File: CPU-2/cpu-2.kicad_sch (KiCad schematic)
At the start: 141 parts, among them Q1 2N2369A, X1 14-Pin Socket, X2 14-Pin Socket, X3 14-Pin Socket, X4 14-Pin Socket, X5 14-Pin Socket, X6 14-Pin Socket

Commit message: Tidied up and added additional Project ORB documents + more KiCAD updates
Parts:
- added D8: 1N4001, Diode_THT:D_DO-41_SOD81_P10.16mm_Horizontal, symbol Sphere:1N4001
- added TSC1, TSC2, TSC3, TSC4, TSC5: ~, symbol Sphere:Jumper_Open
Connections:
- net +5V: now also E14.13 (1C), E25.13, E3.20 (V_{CC}), E3.25 (ENABLE), X1.14 (Φ_{2}), X4.7
- net GNDREF: now also E3.1 (VSS), X4.8, TSC5.
- net at E3.2 (PA0): now also X4.2
- net at E3.3 (PA1): now also X4.3
- net at E3.39 (CA2): now also X4.12
- net at E3.4 (PA2): now also X4.11
- net  32: now reaches E3.40 (CA1)
- net  32: now also TSC1., TSC2., TSC3., TSC4., TSC5.
- net at E3.5 (PA3): now also X4.4
- net at E3.6 (PA4): now also X4.10
- net at E3.7 (PA5): now also X4.5
- net at E3.8 (PA6): now also X4.6
- net at E3.9 (PA7): now also X4.9
- net at E7., E7.8 (Q_{C}): now also TSC3.
- net at E7.1 (CKB): now also E7.12 (Q_{A}), TSC1.
- net at E7.10 (GND): now also TSC4.
- net at E7.9 (Q_{B}): now also TSC2.
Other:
- note added: "RTC"
- moved on the sheet: C7, E3, E7

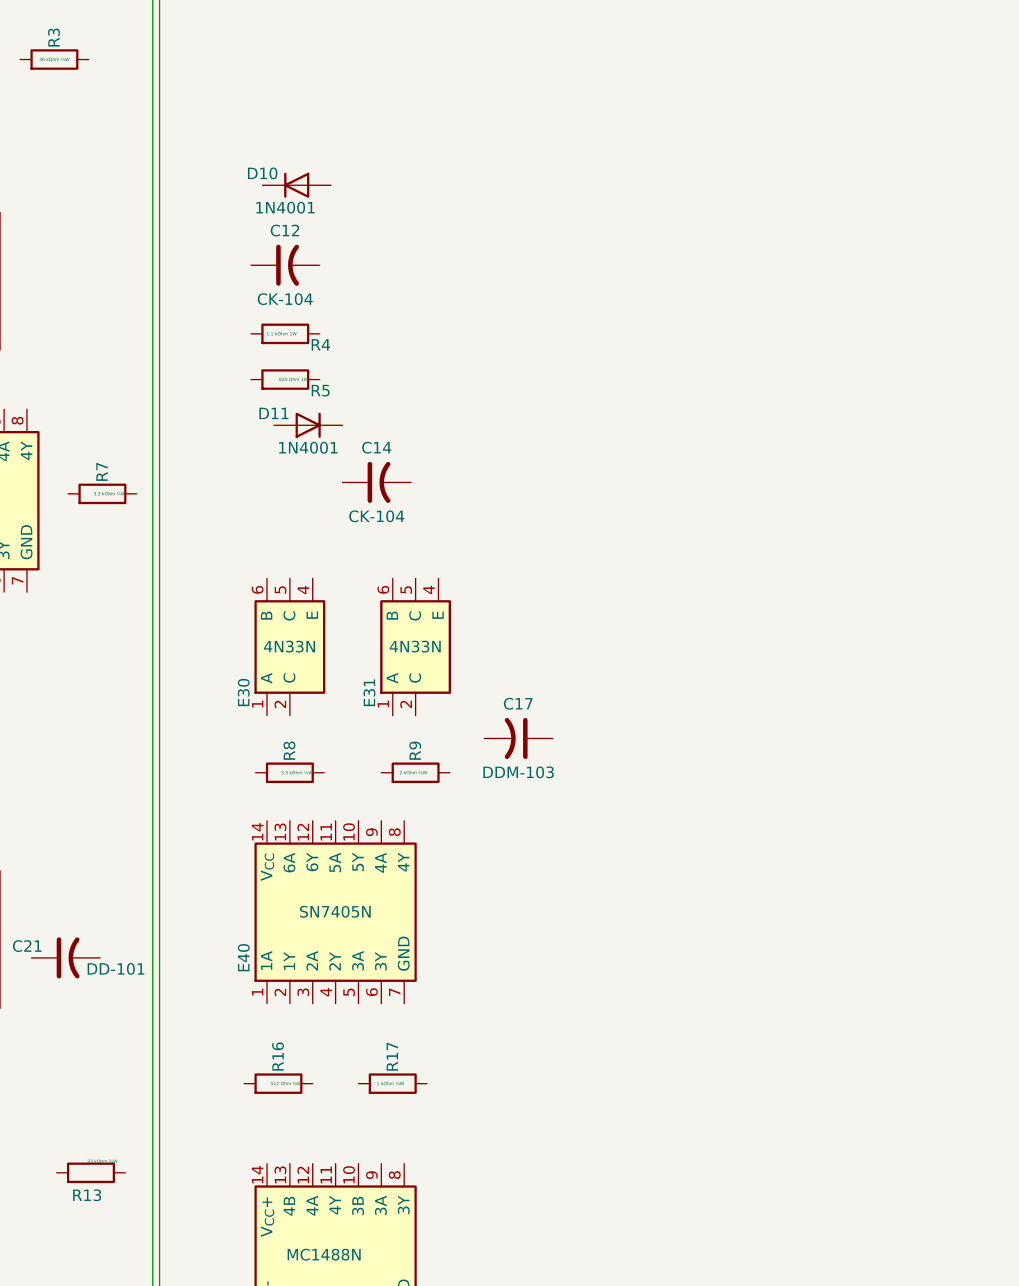
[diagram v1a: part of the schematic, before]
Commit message: Added Project ORB documents and latest KiCAD updates
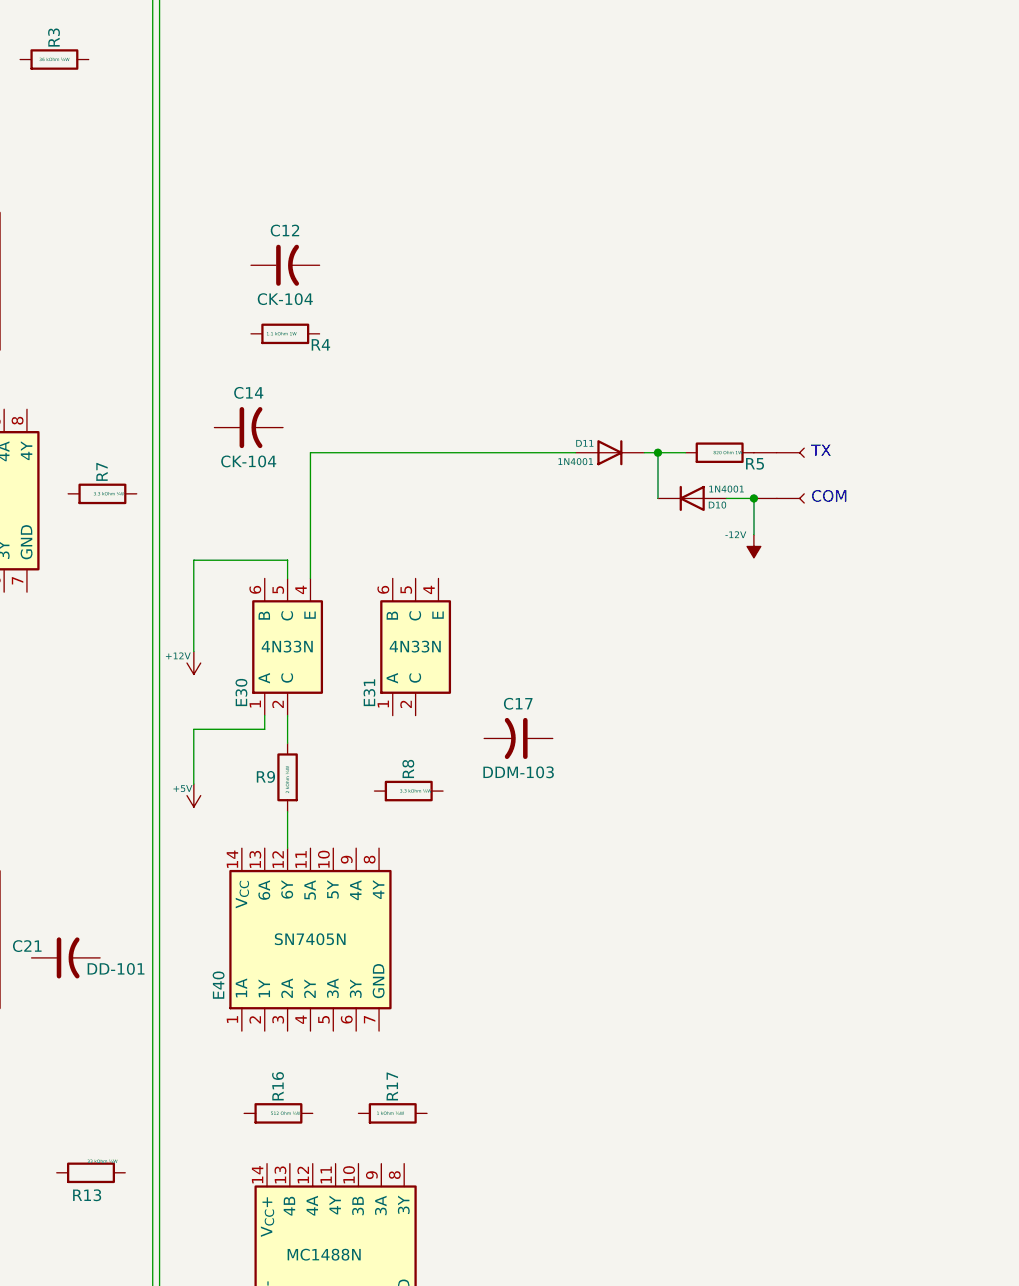
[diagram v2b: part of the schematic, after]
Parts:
- added P5, P6: ~, symbol Sphere:NULL
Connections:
- net +12V: now also E30.5 (C)
- net +5V: now also E30.1 (A)
- net at R5.1: now also D10.1 (K), D11.1 (K)
- net at R5.2: now also P5.0
- net at R9.1: now also E40.12 (6Y)
- net at R9.2: now also E30.2 (C)
- net at E30.4 (E): now also D11.2 (A)
- net -12V: now reaches D10.2 (A)
- net -12V: now also P6.0
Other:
- note added: "COM"
- note added: "TX"
- moved on the sheet: C14, D10, D11, E40, R16, R17, R5, R8, R9

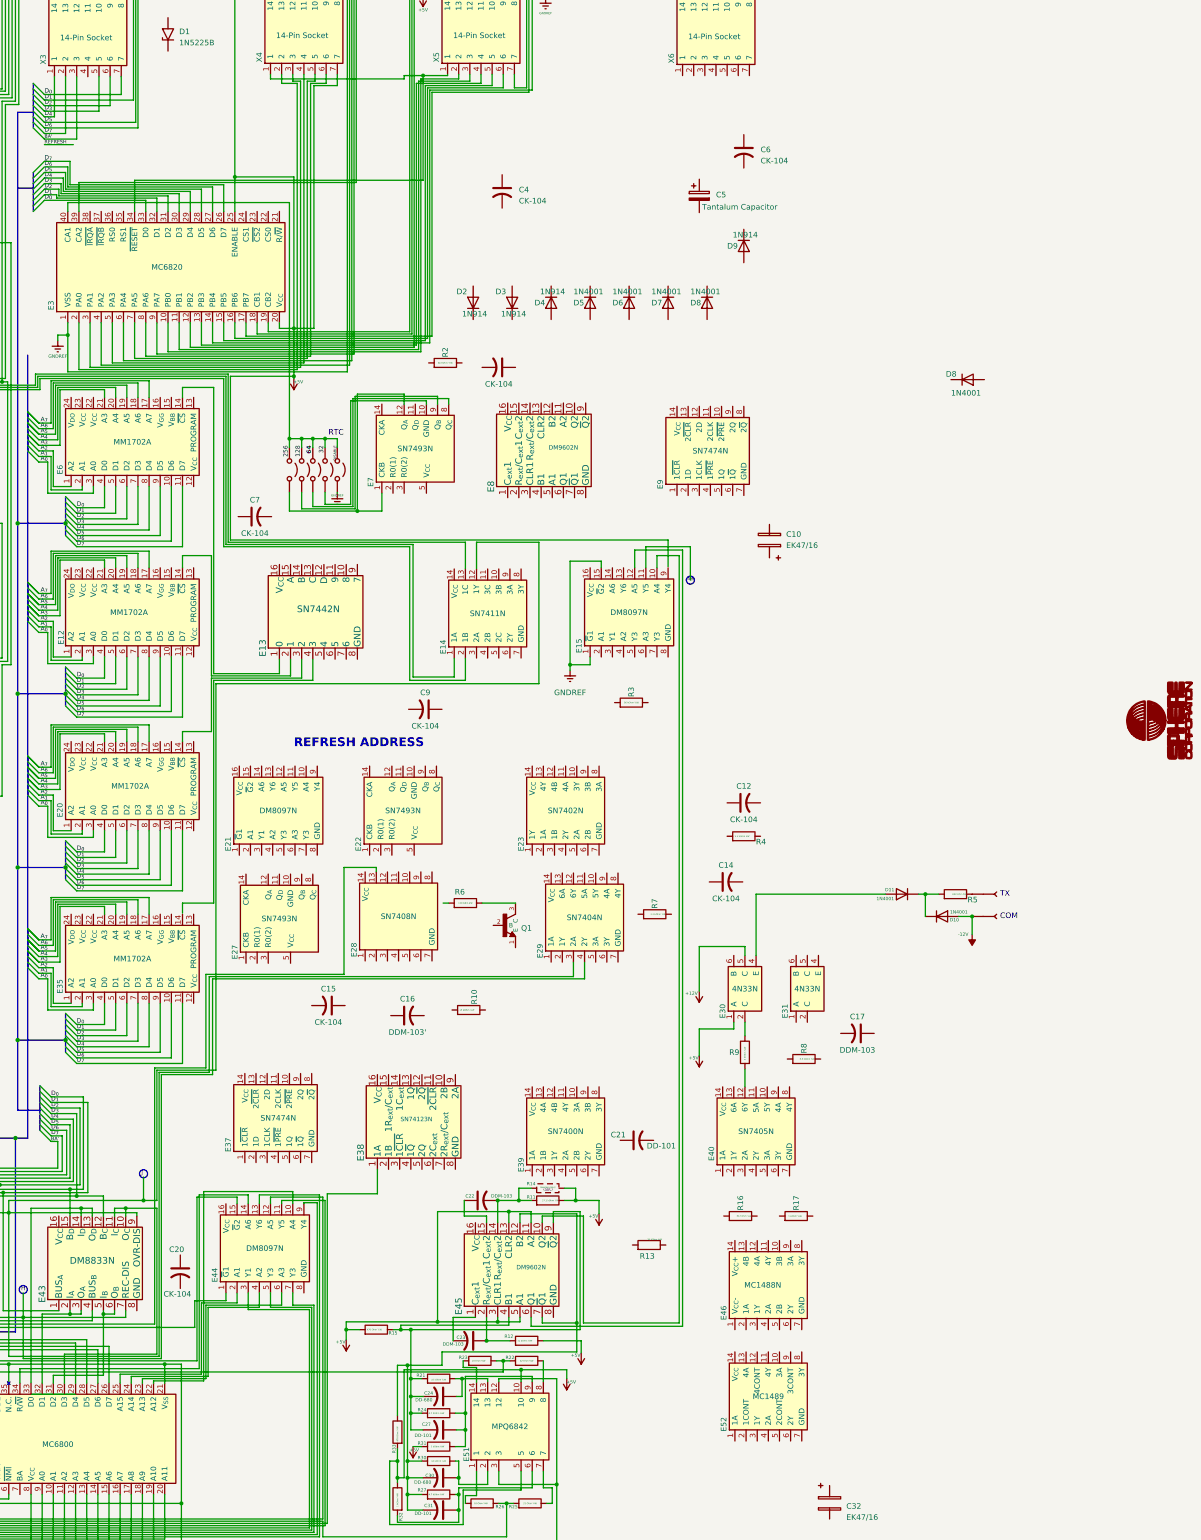
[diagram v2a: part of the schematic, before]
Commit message: CPU/2 Schematic updates
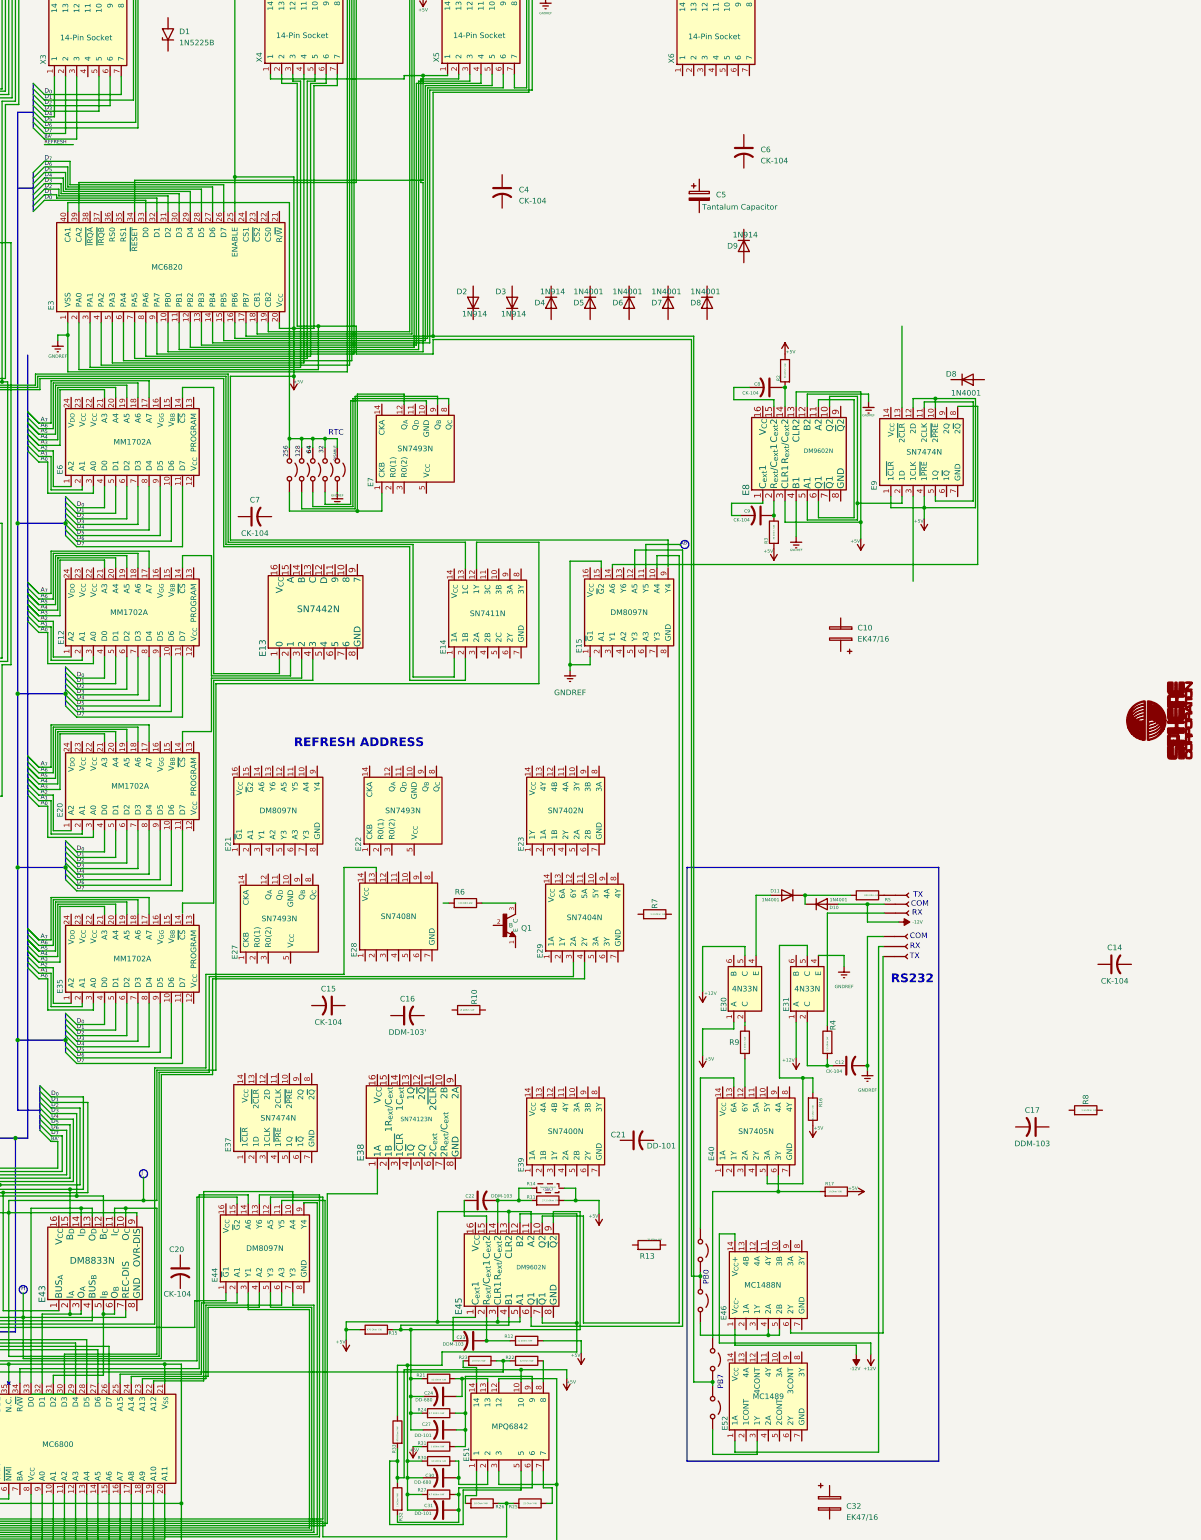
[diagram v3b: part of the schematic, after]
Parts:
- added P10, P7, P8, P9: ~, symbol Sphere:NULL
- added TSC6, TSC7, TSC8, TSC9: ~, symbol Sphere:Jumper_Open
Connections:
- net +12V: now also E31.1 (A), E46.14 (V_{CC}+)
- net +5V: now also E8.13 (CLR2), E8.3 (CLR1), E9.1 (1~{CLR}), E9.10 (2~{PRE}), E9.12 (2D), E9.4 (1~{PRE}), R16.2, R17.2, R2.2, R3.1
- net -12V: now also E46.1 (V_{CC}-)
- net GNDREF: now also C12.2, E31.4 (E), E8.12 (B2), E8.4 (B1), P8.0
- net at E52.1 (1A): now also P9.0
- net at E52.3 (1Y): now also TSC6.
- net at E8.1 (C_{ext}1): now also C9.2
- net at E8.10 (Q2): now also E8.5 (A1), E9.2 (1D)
- net at E8.11 (A2): now also E8.6 (Q1)
- net at E8.14 (R_{ext}/C_{ext}2): now also C8.1, R2.1
- net at E8.15 (C_{ext}2): now also C8.2
- net at E8.2 (R_{ext}/C_{ext}1): now also C9.1, R3.2
- net at E31.2 (C): now also C12.1, R4.1
- net at E31.5 (C): now also E40.5 (3A), R16.1
- net at E40.13 (6A): now also TSC8.
- net at E40.6 (3Y): now also R17.1, TSC7.
- net at E3.17 (PB7), X5.9: now also TSC6., TSC7.
- net at E3.2 (PA0), X4.2: now also TSC8., TSC9.
- net at R4.2: now also P7.0
- net at E46.4 (2A): now also E46.5 (2B), TSC9.
- net at E46.6 (2Y): now also P10.0
- net at E9.11 (2CLK): now also E9.5 (1Q)
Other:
- note added: "PB0"
- note added: "PB7"
- note added: "RS232"
- note added: "RX"
- moved on the sheet: C10, C12, C14, C17, C9, D10, D11, E8, E9, R16, R17, R2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

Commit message: More updates to schematics, books, created RS232 interface project
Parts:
- removed D8: 1N4001, Diode_THT:D_DO-41_SOD81_P10.16mm_Horizontal, symbol Sphere:1N4001
- E30, E31: footprint (none) -> Package_DIP:DIP-6_W10.16mm
- E40, E41, E46, E52: footprint (none) -> Package_DIP:DIP-14_W10.16mm
- renumbered TSC to TSC10
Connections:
- net +12V: now also R6.1
- net +5V: now also D12.1 (K), E38.10 (2B), E38.11 (2~{CLR}), E38.2 (1B), E38.3 (1~{CLR}), E49.13 (4B), R10.2, R13.2, R19.2, R28.1, R7.1; no longer E25.13, E3.20 (V_{CC}), X4.7
- net A_{0}: now also E16.3 (1B)
- net A_{1}: now also E16.2 (1A)
- net A_{2}: now also E24.9 (2A)
- net D_{6}: now also E3.27 (D6)
- net GNDREF: now also C29.2, E44.1 (~{G}1), E47.1 (~{G}1), E47.15 (~{G}2), Q1.1 (E)
- net _{BA'}: no longer E44.1 (~{G}1), E47.1 (~{G}1), E47.15 (~{G}2)
- net at C16.1: now also E38.15 (1R_{ext}/C_{ext}), R10.1
- net at C16.2: now also E38.14 (1C_{ext})
- net at E37.13 (2~{CLR}): now also E39.11 (4Y)
- net at E37.2 (1D): now also E39.8 (3Y)
- net at E37.3 (1CLK): now also E28.12, E9.3 (1CLK)
- net at E16.1 (1Y): now also E24.13 (2D)
- net at R28.2: now also C29.1, D12.2 (A), E49.12 (4A)
- net at E22., E22.8 (Q_{C}): now also E39.13 (4A)
- net at E22.14 (CKA): now also E21.2 (A1), E21.3 (Y1), E27.11 (Q_{D})
- net at E22.2 (R0(1)): now also E22.3 (R0(2)), E27.2 (R0(1)), E27.3 (R0(2)), E28.1, E39.10 (3A)
- net at E15.4 (A2): now also E28.3
- net at E15.5 (Y3): now also X3.4
- net at E28.11: now also E27.14 (CKA)
- net at E28.13, E48.1 (~{G}1), E48.15 (~{G}2): now also E28.2
- net at E28.4: now also E38.12 (2~{Q})
- net at E28.5: now also E32.1 (1A)
- net at E28.6: now also E29.1 (1A)
- net at E28.8: now also Q1.2 (B)
- net at R7.2: now also E39.9 (3B)
- net at E38.6 (2C_{ext}): now also C21.2
- net at E38.7 (2R_{ext}/C_{ext}): now also C21.1, R13.1
- net at E38.9 (2A): now also E32.3 (1Y)
- net _{RW }: now reaches E3.21 (R/~{W})
- net _{A6}: now reaches E3.22 (CS0)
- net _{A6}: now also E24.12 (2C)
- net _{A2}: now reaches E3.23 (~{CS2})
- net at E3.24 (CS1): now also E24.10 (2B)
- net _{A1}: now reaches E3.35 (RS1)
- net _{A0}: now reaches E3.36 (RS0)
- net _{~{IRQ} }: now reaches E3.37 (~{IRQB})
- net _{~{IRQ} }: now also E3.38 (~{IRQA})
- net at E41.10 (5Y): now also E32.2 (1B), E32.4 (2A), R19.1
- net at E41.5 (3A): now also E49.11 (4Y)
- net at E41.6 (3Y): now also E32.10 (3A)
- net at E21.10 (A4): now also E27.9 (Q_{B})
- net at E21.14 (A6): now also E27.1 (CKB), E27.12 (Q_{A})
- net at E21.6 (A3): now also E27., E27.8 (Q_{C})
- net at E4.5 (1D): now also E32.5 (2B)
- net at X3.9: now also E29.6 (3Y)
- net at E32.8 (3Y): now also E7.2 (R0(1)), E7.3 (R0(2))
- new net: E3.20 (V_{CC}), X4.7
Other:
- note added: "0.1 27-MAR-2023 Andrew Shapton Initial Version"
- note added: "CE"
- note added: "G"
- note added: "NOTES"
- note added: "R/W MODIFIER"
- note added: "REVISION HISTORY"
- note added: "RW'"
- note added: "TRI-S"
- note added: "The original schematic separates chip pins out for ease of diagramming. This version does not"
- note added: "This schematic includes the RS232 interface, which is not the default on the CPU/2 board"
- note added: "~{CS}"
- company: Sphere Computer -> (none)
- moved on the sheet: C1, C10, C11, C12, C13, C14, C15, C16, C17, C18, C19, C2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
